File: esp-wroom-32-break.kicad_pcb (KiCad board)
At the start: 2 copper layers, 10.2 x 1.9 mm, 15 parts, among them CON1 Micro_SD_Card, IC1 FT232RQ, P1 CONN_01X18, P2 CONN_01X18, P3 USB_OTG, P4 Switch, U1 ESP32-WROOM, U2 NJU7223DL1-33

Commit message: Put footprints
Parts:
- added C6: 0.1uf, Capacitors_SMD:C_0603, F.Cu at (177.8, 104.1)
- added C7: 4.7uf, Capacitors_SMD:C_0603, F.Cu at (181.6, 104.1)
- IC1: footprint ftdi4:ftdi4-QFN-32 -> ftdi232rq:ft232rq
- P4: moved to B.Cu
- moved D1 74.1 mm to (185.4, 111.8), turned to 180 degrees
- moved C1 72.3 mm to (177.8, 109.2), turned to 180 degrees
- moved R1 71.4 mm to (177.8, 106.7), turned to 180 degrees
- moved C3 71.1 mm to (181.6, 106.7)
- moved CON1 70.9 mm to (166.4, 113.0)
- moved C4 62.8 mm to (185.4, 109.2), turned to 180 degrees
- moved P4 50.0 mm to (180.3, 118.1), turned to 180 degrees
- moved U1 39.4 mm to (167.6, 73.7), turned to 180 degrees
- moved C2 38.6 mm to (181.6, 109.2)
- moved P3 37.2 mm to (180.3, 121.9)
- moved IC1 31.6 mm to (170.4, 96.5)
- moved P1 28.7 mm to (149.9, 68.6)
- moved C5 21.2 mm to (185.4, 106.7), turned to 180 degrees
- moved U2 20.7 mm to (180.6, 100.3)
- moved P2 2.14 mm to (190.5, 68.6)
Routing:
- net GND: track 0.00 -> 284.3 mm, vias 0 -> 32
- net +3V3: track 0.00 -> 147.2 mm, vias 0 -> 4
- net EN: track 0.00 -> 54.8 mm, vias 0 -> 2
- net boot: track 0.00 -> 41.9 mm, vias 0 -> 1
- net RXDtoTXD0: track 0.00 -> 31.1 mm, vias 0 -> 2
- net TXDtoRXD0: track 0.00 -> 26.5 mm, vias 0 -> 2
- net IO15: track 0.00 -> 26.1 mm
- net VCC: track 0.00 -> 24.2 mm
- net IO13: track 0.00 -> 23.3 mm
- net SD1: track 0.00 -> 22.9 mm
- net SD2: track 0.00 -> 22.2 mm, vias 0 -> 2
- net IO2: track 0.00 -> 22.1 mm
- net SD0: track 0.00 -> 22.0 mm, vias 0 -> 2
- net SD_CLK: track 0.00 -> 20.7 mm, vias 0 -> 2
- net IO12: track 0.00 -> 20.3 mm
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- added copper zone on B.Cu, net GND
- added copper zone on F.Cu, net GND
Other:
- board size 10.2 x 1.9 mm -> 43.2 x 61 mm

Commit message: Created revision 1.0 pcb
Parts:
- added G***: LOGO, osh-logo:osh-logo-3p4mm, B.Cu at (150.9, 64.0)
- added REF***: OSHW-Logo_5.7x6mm_SilkScreen, Symbols:OSHW-Logo_5.7x6mm_SilkScreen, F.Cu at (156.0, 100.8)
- moved U1 2.54 mm to (170.2, 73.7)
- moved P3 1.91 mm to (178.4, 121.9)
- moved P4 1.91 mm to (178.4, 118.1)
- moved CON1 1.27 mm to (165.1, 113.0)
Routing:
- net GND: track 284.3 -> 266.3 mm
- net IO4: track 18.1 -> 14.6 mm
- net IO26: track 17.1 -> 19.9 mm
- net SVN: track 11.0 -> 13.7 mm
- net IO33: track 14.5 -> 17.3 mm
- net IO32: track 13.3 -> 16.1 mm
- net IO27: track 18.4 -> 21.1 mm
- net SVP: track 10.4 -> 13.2 mm
- net IO35: track 12.0 -> 14.8 mm
- net IO14: track 19.6 -> 22.4 mm
- net IO34: track 11.5 -> 14.3 mm
- net RXDtoTXD0: track 31.1 -> 33.6 mm
- net TXDtoRXD0: track 26.5 -> 29.0 mm
- net IO25: track 15.7 -> 18.2 mm
- net IO2: track 22.1 -> 19.5 mm
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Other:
- board size 43.2 x 61 mm -> 45.7 x 61 mm
- board text added: "3V3"
- board text added: "BOOT"
- board text added: "D04"
- board text added: "D05"
- board text added: "D12"
- board text added: "D13"
- board text added: "D14"
- board text added: "D15"
- board text added: "D16"
- board text added: "D17"
- board text added: "D18"
- board text added: "D19"
- board text added: "D21"
- board text added: "D22"
- board text added: "D23"
- board text added: "D25"
- board text added: "D26"
- board text added: "D27"
- board text added: "D32"
- board text added: "D33"
- board text added: "D34"
- board text added: "D35"
- board text added: "EN"
- board text added: "ESP32BB"
- board text added: "GND"
- board text added: "Rev 1.0"
- board text added: "SVN"
- board text added: "SVP"
- board text added: "VCC"
- board text added: "github.com/asukiaaa/esp32bb"

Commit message: Correct pin name on back silk
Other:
- board text added: "D02"
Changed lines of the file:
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@@
     (links 89)
     (no_connects 1)
-    (area 147.244999 60.884999 193.115001 121.995001)
+    (area 143.958381 58.461 195.533334 124.695)
     (thickness 1.6)
-    (drawings 53)
+    (drawings 54)
     (tracks 392)
     (zones 0)
@@
       (drillshape 0)
       (scaleselection 1)
-      (outputdirectory plots/))
+      (outputdirectory silks/))
   )
   (net 0 "")
@@
       (xy 0.376964 -2.709982)) (layer F.SilkS) (width 0.01))
   )
+  (gr_text GND (at 192.3542 68.58 90) (layer B.SilkS)
+    (effects (font (size 0.7 0.7) (thickness 0.175)) (justify mirror))
+  )
   (gr_text "Rev 1.0" (at 156.21 93.472) (layer F.SilkS)
     (effects (font (size 1 1) (thickness 0.2)))
@@
     (effects (font (size 0.7 0.7) (thickness 0.175)) (justify mirror))
   )
-  (gr_text D15 (at 192.405 96.52 90) (layer B.SilkS)
+  (gr_text D02 (at 192.405 96.52 90) (layer B.SilkS)
     (effects (font (size 0.7 0.7) (thickness 0.175)) (justify mirror))
   )

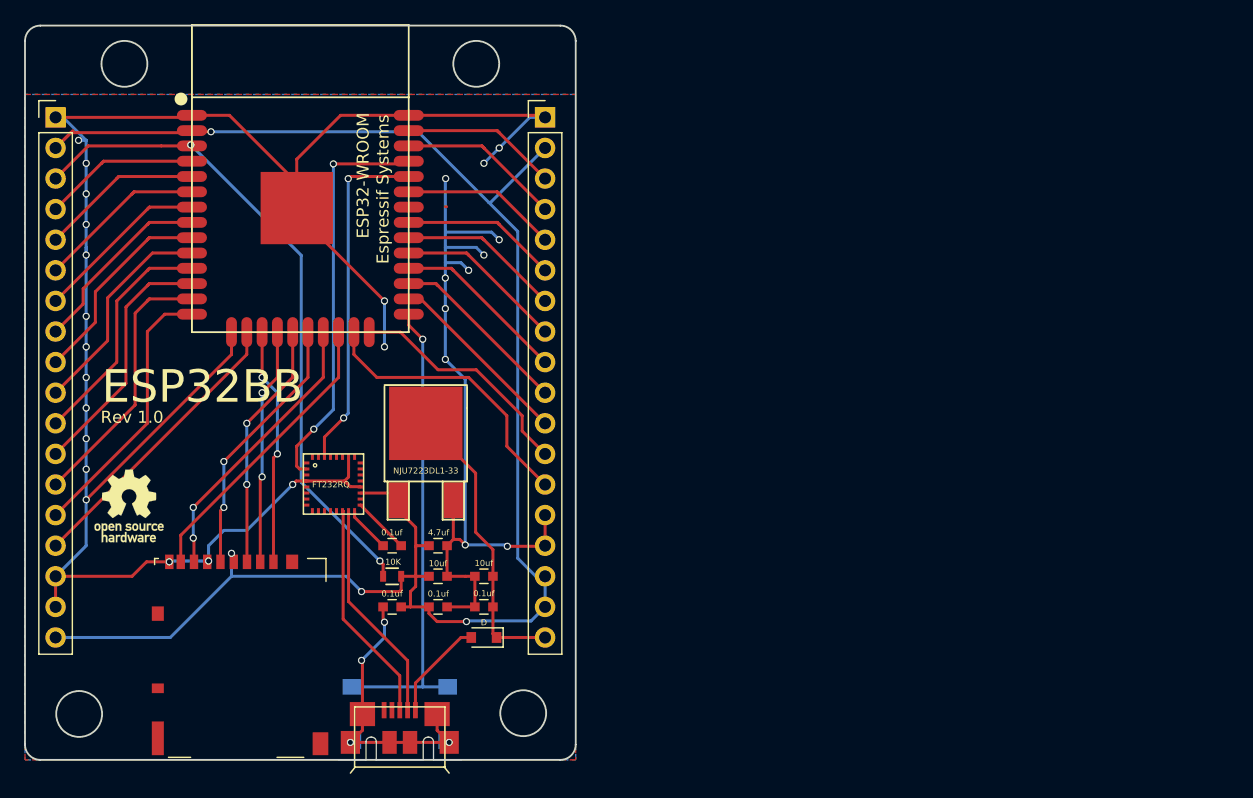
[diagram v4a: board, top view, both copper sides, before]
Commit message: Put footprints for rev1.1
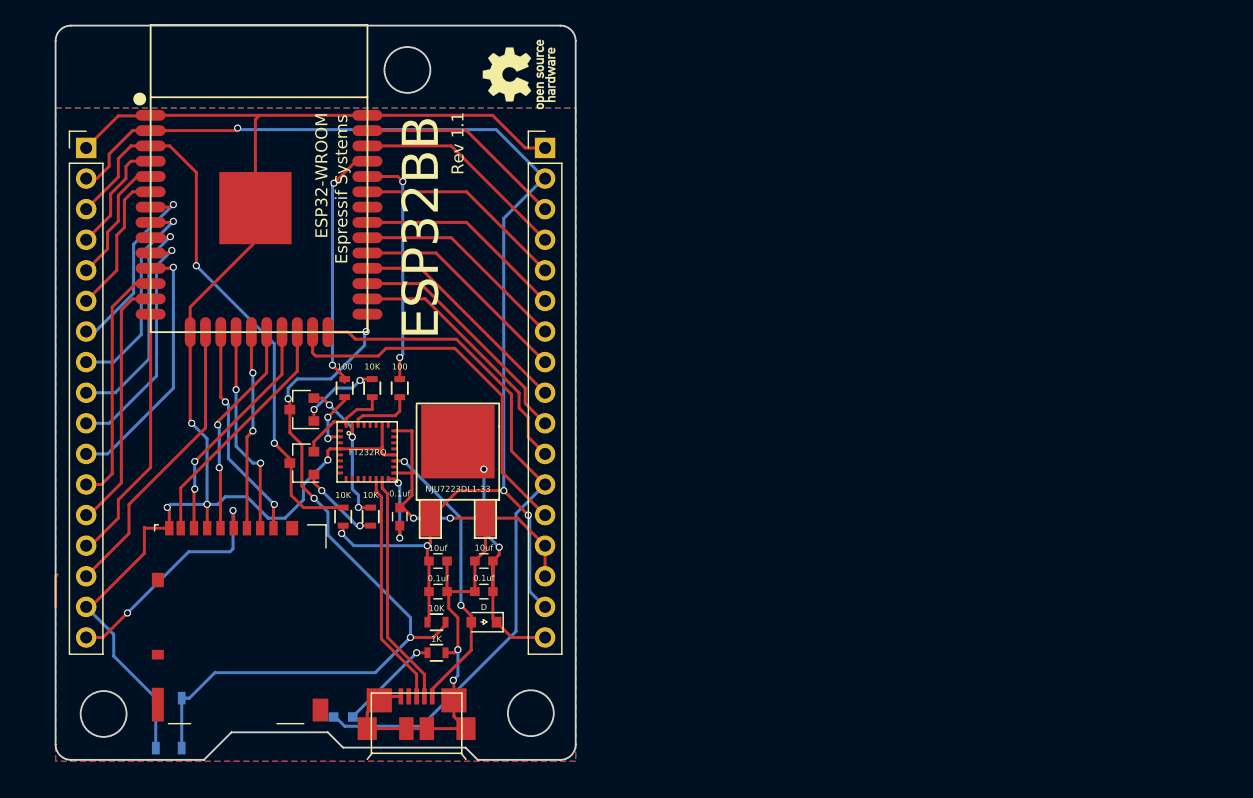
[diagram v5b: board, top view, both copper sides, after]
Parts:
- removed C1: 0.1uf, Capacitors_SMD:C_0603
- removed C7: 4.7uf, Capacitors_SMD:C_0603
- removed P4: Switch, Buttons_Switches_SMD:SW_SPST_B3S-1000
- added D2: LED, common:LED_0603, B.Cu at (173.7, 118.4)
- added Q1: MMBT3904, TO_SOT_Packages_SMD:SOT-23, F.Cu at (170.3, 97.3)
- added Q2: MMBT3904, TO_SOT_Packages_SMD:SOT-23, F.Cu at (170.3, 92.8)
- added R2: 10K, Resistors_SMD:R_0603, F.Cu at (181.5, 110.5)
- added R3: 10K, Resistors_SMD:R_0603, F.Cu at (173.7, 101.7)
- added R4: 100, Resistors_SMD:R_0603, F.Cu at (178.4, 91.1)
- added R5: 100, Resistors_SMD:R_0603, F.Cu at (173.9, 91.1)
- added R6: 10K, Resistors_SMD:R_0603, F.Cu at (176.1, 91.1)
- added R7: 1K, Resistors_SMD:R_0603, F.Cu at (181.5, 113.0)
- added SW1: SWITCH_SPST, switch:SKRPACE010, B.Cu at (159.3, 118.9)
- D1: footprint Diodes_SMD:D_0805 -> common:D_0805
- P1, P2: value CONN_01X18 -> CONN_01X17; footprint Pin_Headers:Pin_Header_Straight_1x18_Pitch2.54mm -> Pin_Headers:Pin_Header_Straight_1x17_Pitch2.54mm
- moved REF*** 48.3 mm to (188.3, 65.0), turned to 90 degrees
- moved G*** 38.7 mm to (189.6, 64.1)
- moved R1 5.26 mm to (176.0, 101.7), turned to 270 degrees
- moved IC1 3.86 mm to (173.2, 93.9)
- moved P1 3.59 mm to (152.4, 71.1)
- moved U1 3.43 mm to (166.8, 73.7)
- moved U2 3.07 mm to (183.3, 101.9)
- moved CON1 2.79 mm to (165.1, 110.2)
- moved P2 2.54 mm to (190.5, 71.1)
- moved C6 2.50 mm to (178.4, 101.7), turned to 90 degrees
- moved P3 1.81 mm to (179.8, 120.8)
- moved C3 1.27 mm to (181.6, 105.4)
- moved C5 1.27 mm to (185.4, 105.4)
- moved D1 1.27 mm to (185.4, 110.5)
- moved C2 1.27 mm to (181.6, 108.0)
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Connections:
- IC1 pad 19: +3V3 -> +5V
- IC1 pad 2: RXDtoTXD0 -> Net-(IC1-Pad2)
- IC1 pad 30: TXDtoRXD0 -> Net-(IC1-Pad30)
- IC1 pad 31: Net-(IC1-Pad31) -> DTR
- IC1 pad 32: Net-(IC1-Pad32) -> RTS
- P1 pad 17: GND -> +3V3
- P2 pad 17: +3V3 -> VCC
- R1 pad 1: +3V3 -> DTR
- R1 pad 2: EN -> Net-(Q1-Pad1)
- U1 pad 25: boot -> IO0(boot)
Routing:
- net GND: track 266.3 -> 194.7 mm, vias 32 -> 8
- net IO0(boot): track 0.00 -> 64.2 mm, vias 0 -> 4
- net boot: track 39.4 -> 0.00 mm, vias 1 -> 0
- net IO2: track 19.5 -> 57.9 mm
- net +3V3: track 149.0 -> 124.7 mm, vias 4 -> 7
- net +5V: track 8.46 -> 24.0 mm, vias 0 -> 2
- net DTR: track 0.00 -> 13.1 mm, vias 0 -> 3
- net RXDtoTXD0: track 33.6 -> 20.8 mm
- net TXDtoRXD0: track 29.0 -> 19.6 mm
- net Net-(D2-Pad1): track 0.00 -> 8.43 mm, vias 0 -> 1
- net RTS: track 0.00 -> 8.42 mm
- net IO4: track 14.6 -> 21.8 mm
- net IO15: track 23.7 -> 30.9 mm
- net Net-(Q2-Pad1): track 0.00 -> 6.97 mm, vias 0 -> 2
- net Net-(Q1-Pad1): track 0.00 -> 6.88 mm, vias 0 -> 2
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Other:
- board size 45.7 x 61 mm -> 43.2 x 61 mm
- board text added: "D01 PULLUP"
- board text added: "Rev 1.1"
- board text removed: "BOOT"
- board text removed: "Rev 1.0"

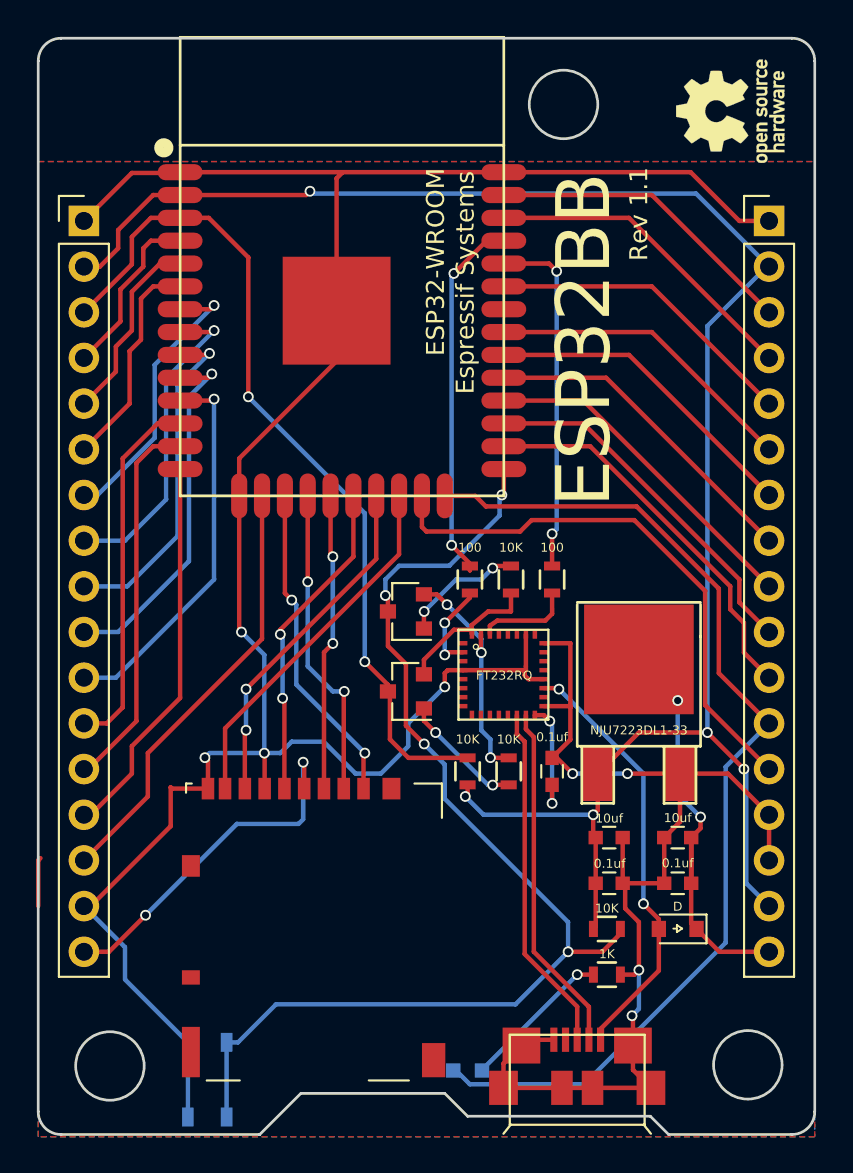
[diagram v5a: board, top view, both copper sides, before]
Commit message: Change led and silk layout
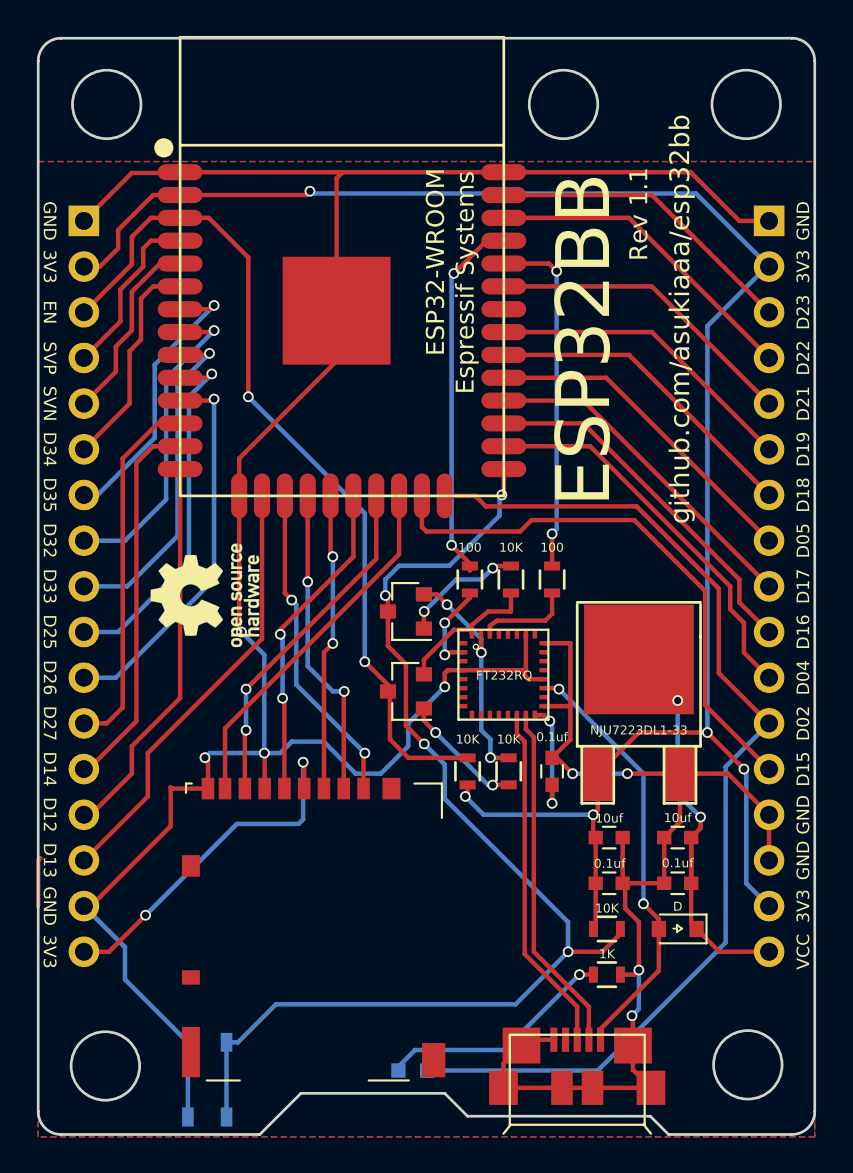
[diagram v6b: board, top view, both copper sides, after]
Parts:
- P1, P2: footprint Pin_Headers:Pin_Header_Straight_1x17_Pitch2.54mm -> common:Pin_Header_Straight_1x17_Pitch2.54mm
- moved REF*** 39.7 mm to (159.1, 91.9)
- moved G*** 23.6 mm to (166.0, 64.5)
- moved D2 3.05 mm to (170.7, 118.4), turned to 0 degrees
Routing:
- net Net-(D2-Pad1): track 8.43 -> 13.2 mm
- net IO2: track 57.9 -> 58.8 mm
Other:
- outline, holes or cut-outs redrawn
